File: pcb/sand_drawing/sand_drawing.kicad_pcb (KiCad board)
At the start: 2 copper layers, 54.2 x 81.5 mm, 41 parts, among them J0 12V GND, J1 Stepper1, J2 Stepper2, J3 Opto 1, J4 Opto 2, J5 UART, SW1 EN, SW2 IO0, U1 AP63203WU, U2 ESP32-WROOM-32D

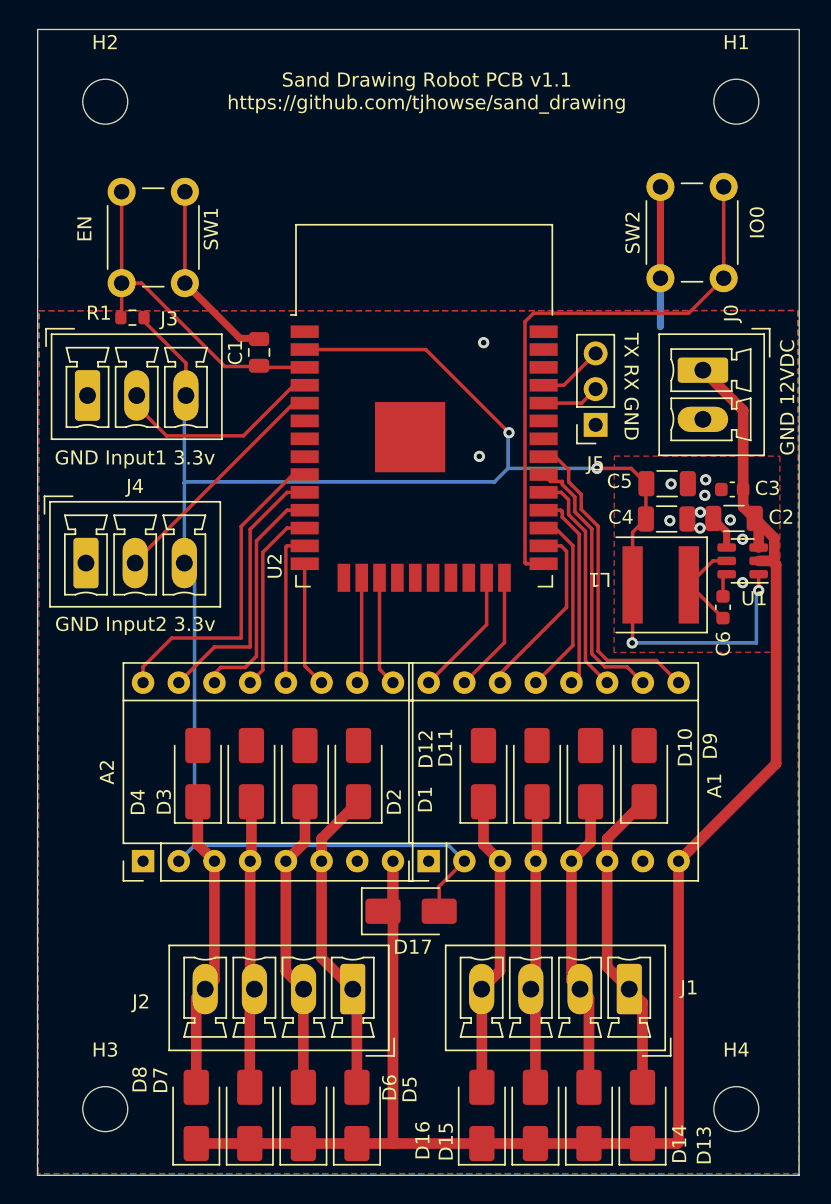
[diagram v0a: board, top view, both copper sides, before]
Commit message: Minor tweaks to PCB. Thicker 12v rail, rearranged 3.3v connection to drivers, thicker connection between PSU and inductor.
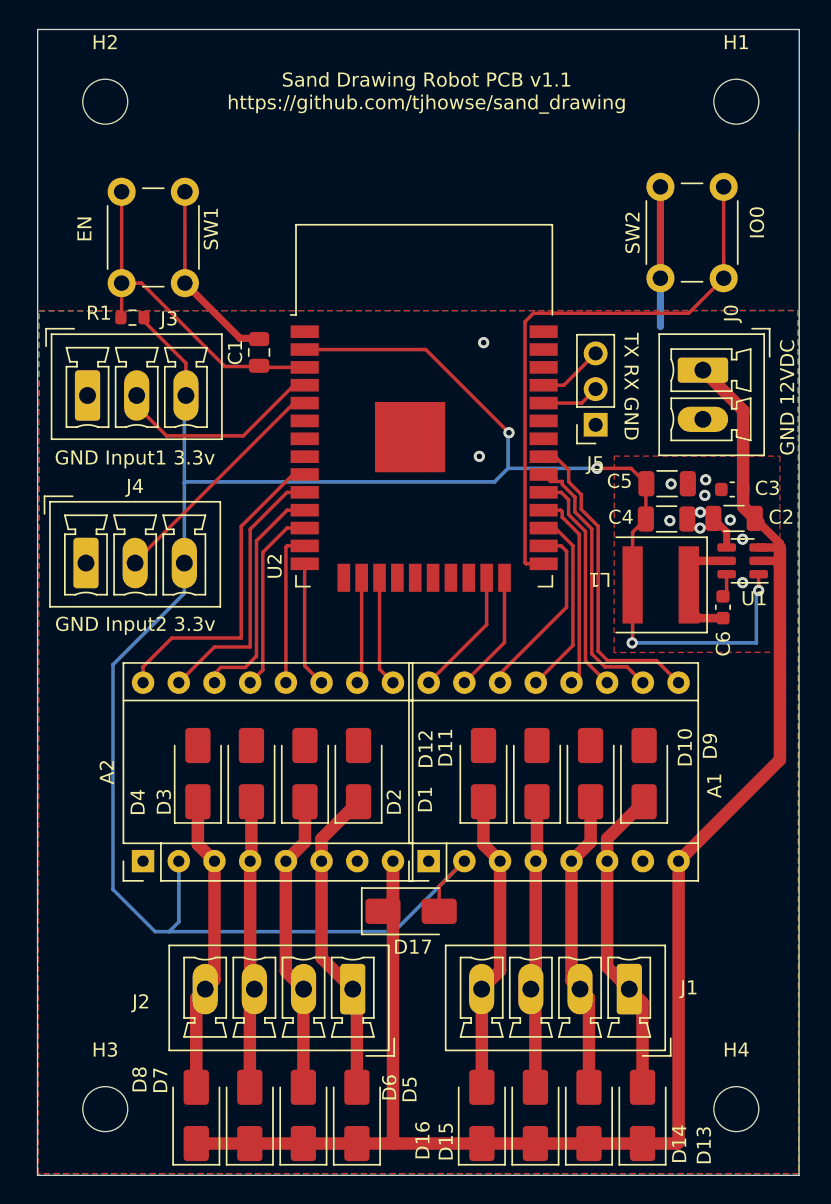
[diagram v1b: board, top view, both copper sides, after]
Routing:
- net +3V3: track 143.4 -> 161.7 mm
- net Net-(U1-SW): track 6.81 -> 5.57 mm

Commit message: Tweaks to PCB. Finding parts.
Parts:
- D1, D10, D11, D12, D13, D14, D15, D16, D17, D2, D3, D4, D5, D6, D7, D8, D9: value SS210 Schottky Diode -> 100V 850mV@2A Schottky Diode

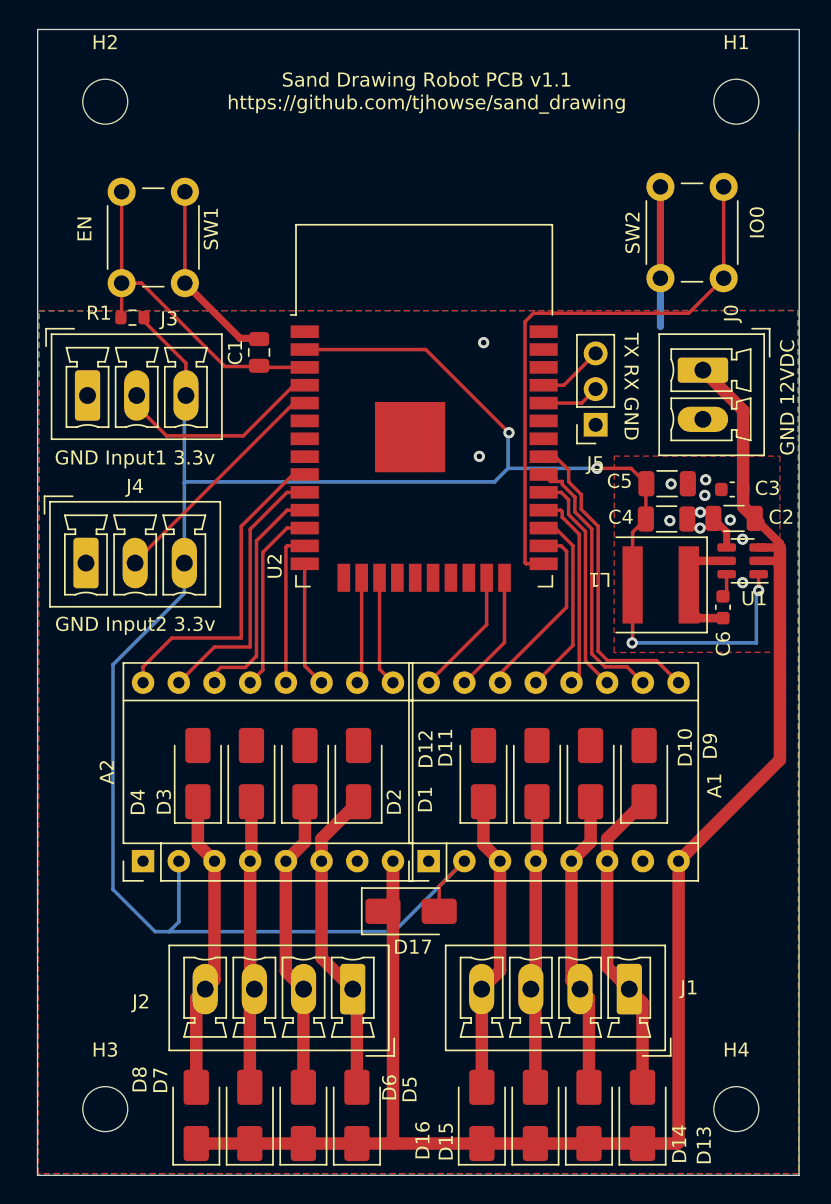
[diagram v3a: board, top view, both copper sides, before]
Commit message: Updated part numbers and footprints.
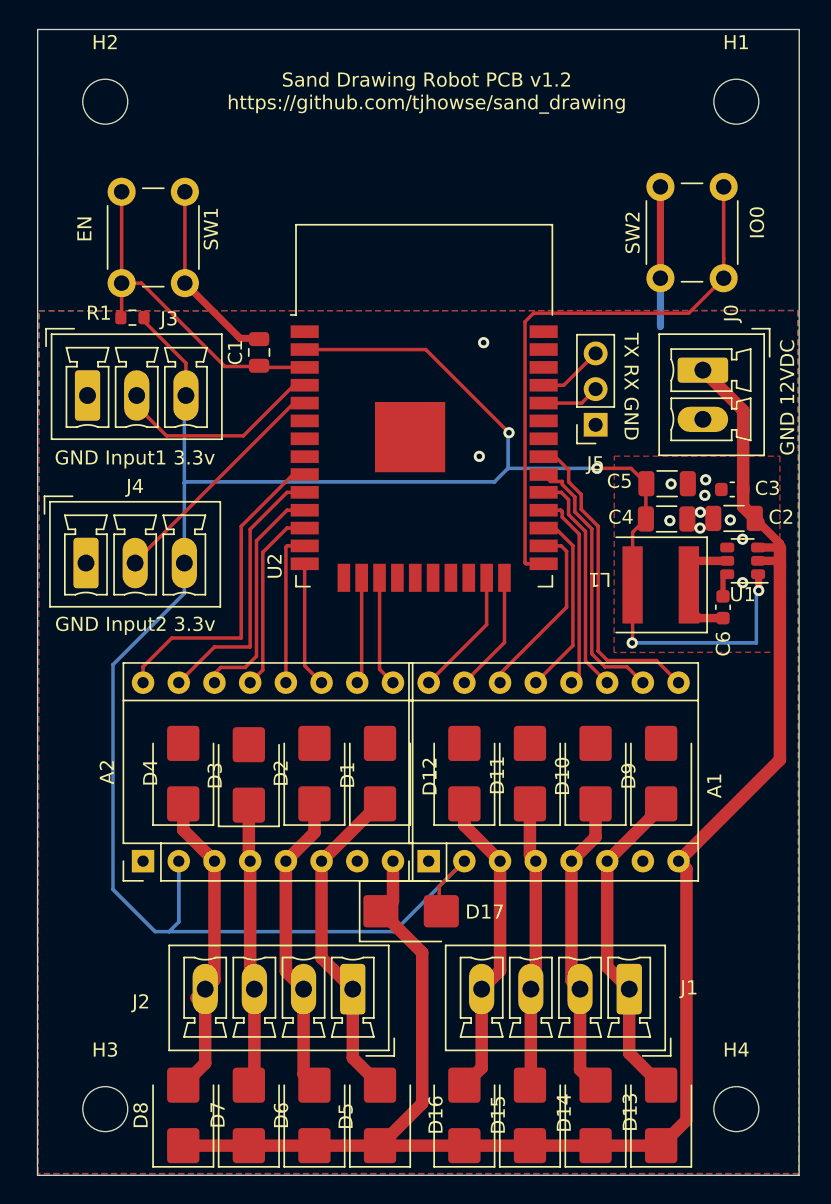
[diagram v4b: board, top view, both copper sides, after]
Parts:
- C1: value 100pF/50V -> 50V 100pF ±5%
- C2: value 10µF/35V -> 10µF/35V ±10%
- C3, C6: value 100nF/50V -> 100nF/50V ±10%
- C4, C5: value 22µF/25V -> 22µF/25V ±20%
- D1, D10, D11, D12, D13, D14, D15, D16, D17, D2, D3, D4, D5, D6, D7, D8, D9: footprint Diode_SMD:D_SMA -> Diode_SMD:D_SMB
- R1: value 10k -> 10k 1% 0.25W
- U1: footprint Package_TO_SOT_SMD:TSOT-23-6 -> sand_drawing_parts:TSOT-26-6
- moved D5 1.64 mm to (121.0, 152.1)
- moved D1 1.53 mm to (121.0, 127.8)
- moved D12 1.36 mm to (127.0, 127.8)
- moved D13 1.32 mm to (141.0, 152.1)
- moved D16 1.25 mm to (127.0, 152.1)
- moved D9 1.21 mm to (141.0, 127.8)
- moved D4 1.04 mm to (107.0, 127.8)
- moved D8 0.92 mm to (107.0, 152.1)
- moved D6 0.79 mm to (116.3, 152.1)
- moved D2 0.67 mm to (116.3, 127.8)
- moved D11 0.50 mm to (131.7, 127.8)
- moved D14 0.47 mm to (136.3, 152.1)
- moved D15 0.39 mm to (131.7, 152.1)
- moved D10 0.35 mm to (136.3, 127.8)
- moved D3 0.21 mm to (111.7, 127.8)
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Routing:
- net GND: track 25.8 -> 23.3 mm
- net Net-(A2-B2): track 22.4 -> 23.9 mm
- net Net-(A2-A2): track 21.3 -> 22.8 mm
- net Net-(A1-A2): track 21.4 -> 22.1 mm
- net Net-(A1-B2): track 22.4 -> 23.2 mm
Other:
- board text added: "Sand Drawing Robot PCB v1.2 https://github.com/tjhowse/sand_drawing"
- board text removed: "Sand Drawing Robot PCB v1.1 https://github.com/tjhowse/sand_drawing"
